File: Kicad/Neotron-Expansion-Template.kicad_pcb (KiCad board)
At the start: 2 copper layers, 100 x 50 mm, 26 parts, among them J1 Neotron-Expansion-Edge, SW1 SW_DIP_x08, U1 MCP23S17, U2 34LC02

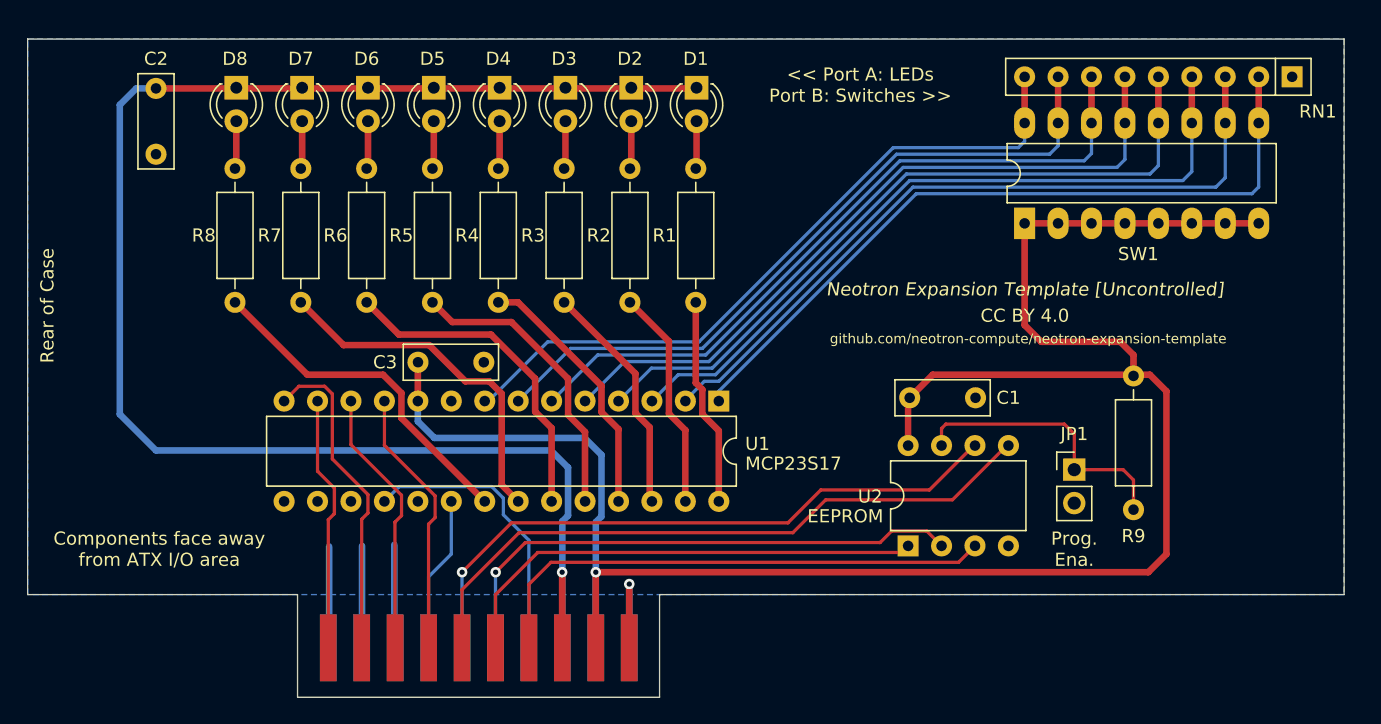
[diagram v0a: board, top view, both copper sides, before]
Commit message: Updated to KiCAD 6 and re-worked.
Power is the right way around now....
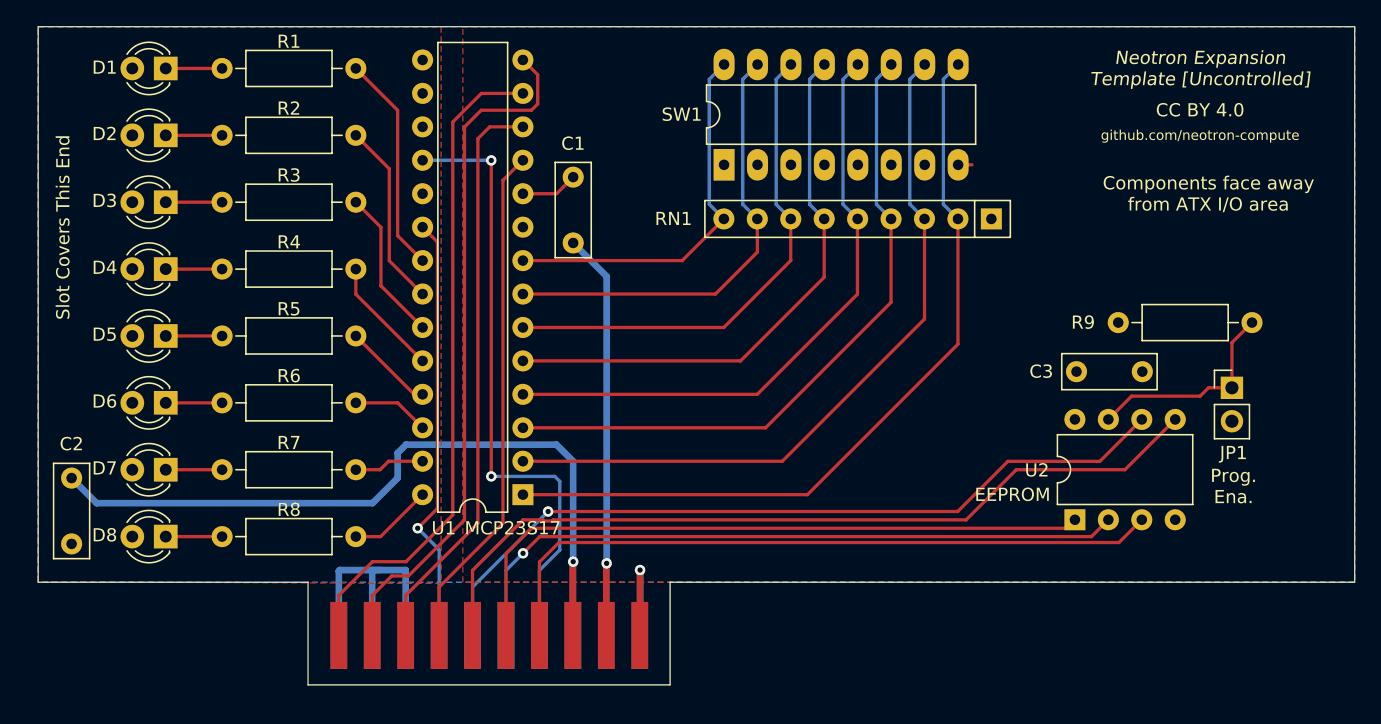
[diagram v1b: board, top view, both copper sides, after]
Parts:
- RN1: value 10k x 8 -> 10k
- moved D1 40.3 mm to (60.5, 102.2), turned to 180 degrees
- moved D2 35.5 mm to (60.5, 107.3), turned to 180 degrees
- moved D8 34.5 mm to (60.5, 137.8), turned to 180 degrees
- moved D3 31.6 mm to (60.5, 112.4), turned to 180 degrees
- moved R1 31.3 mm to (74.9, 102.2), turned to 180 degrees
- moved D7 30.8 mm to (60.5, 132.7), turned to 180 degrees
- moved C2 30.3 mm to (53.3, 133.3)
- moved D4 28.9 mm to (60.5, 117.5), turned to 180 degrees
- moved D6 28.4 mm to (60.5, 127.6), turned to 180 degrees
- moved D5 27.7 mm to (60.5, 122.6), turned to 180 degrees
- moved RN1 25.3 mm to (123.2, 113.7)
- moved R2 24.4 mm to (74.9, 107.3), turned to 180 degrees
- moved SW1 23.3 mm to (102.9, 109.6)
- moved R8 20.0 mm to (74.9, 137.8), turned to 180 degrees
- moved R3 17.6 mm to (74.9, 112.4), turned to 180 degrees
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- renumbered C3 to C1, C1 to C3
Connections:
- net /I2C_SCL renamed /SCL
- net /I2C_SDA renamed /SDA
- net Net-(J1-Pad1) renamed /COPI
- net Net-(J1-Pad14) renamed /~{RESET}
- net Net-(J1-Pad3) renamed /CIPO
- net Net-(J1-Pad5) renamed /CLK
- net Net-(J1-Pad7) renamed /~{CS}
- net Net-(J1-Pad8) renamed /~{IRQ}
- net Net-(JP1-Pad1) renamed /WP
- net Net-(RN1-Pad2) renamed /B0
- net Net-(RN1-Pad3) renamed /B1
- net Net-(RN1-Pad4) renamed /B2
- net Net-(RN1-Pad5) renamed /B3
- net Net-(RN1-Pad6) renamed /B4
- net Net-(RN1-Pad7) renamed /B5
- net Net-(RN1-Pad8) renamed /B6
- net Net-(RN1-Pad9) renamed /B7
- D1 pad 1: +5V -> Net-(R1-Pad2)
- D1 pad 2: Net-(D1-Pad2) -> +5V
- D2 pad 1: +5V -> Net-(D2-Pad1)
- D2 pad 2: Net-(D2-Pad2) -> +5V
- D3 pad 1: +5V -> Net-(D3-Pad1)
- D3 pad 2: Net-(D3-Pad2) -> +5V
- D4 pad 1: +5V -> Net-(D4-Pad1)
- D4 pad 2: Net-(D4-Pad2) -> +5V
- D5 pad 1: +5V -> Net-(D5-Pad1)
- D5 pad 2: Net-(D5-Pad2) -> +5V
- D6 pad 1: +5V -> Net-(D6-Pad1)
- D6 pad 2: Net-(D6-Pad2) -> +5V
- D7 pad 1: +5V -> Net-(D7-Pad1)
- D7 pad 2: Net-(D7-Pad2) -> +5V
- D8 pad 1: +5V -> Net-(D8-Pad1)
- D8 pad 2: Net-(D8-Pad2) -> +5V
- R1 pad 1: Net-(R1-Pad1) -> /A0
- R1 pad 2: Net-(D1-Pad2) -> Net-(R1-Pad2)
- R2 pad 1: Net-(R2-Pad1) -> /A1
- R2 pad 2: Net-(D2-Pad2) -> Net-(D2-Pad1)
- R3 pad 1: Net-(R3-Pad1) -> /A2
- R3 pad 2: Net-(D3-Pad2) -> Net-(D3-Pad1)
- R4 pad 1: Net-(R4-Pad1) -> /A3
- R4 pad 2: Net-(D4-Pad2) -> Net-(D4-Pad1)
- R5 pad 1: Net-(R5-Pad1) -> /A4
- R5 pad 2: Net-(D5-Pad2) -> Net-(D5-Pad1)
- R6 pad 1: Net-(R6-Pad1) -> /A5
- R6 pad 2: Net-(D6-Pad2) -> Net-(D6-Pad1)
- R7 pad 1: Net-(R7-Pad1) -> /A6
- R7 pad 2: Net-(D7-Pad2) -> Net-(D7-Pad1)
- R8 pad 1: Net-(R8-Pad1) -> /A7
- R8 pad 2: Net-(D8-Pad2) -> Net-(D8-Pad1)
- U1 pad 10: +3V3 -> GND
- U1 pad 19: (no net) -> unconnected-(U1-Pad19)
- U1 pad 21: Net-(R8-Pad1) -> /A0
- U1 pad 22: Net-(R7-Pad1) -> /A1
- U1 pad 23: Net-(R6-Pad1) -> /A2
- U1 pad 24: Net-(R5-Pad1) -> /A3
- U1 pad 25: Net-(R4-Pad1) -> /A4
- U1 pad 26: Net-(R3-Pad1) -> /A5
- U1 pad 27: Net-(R2-Pad1) -> /A6
- U1 pad 28: Net-(R1-Pad1) -> /A7
- U1 pad 9: GND -> +3V3
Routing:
- net +3V3: track 157.9 -> 37.4 mm
- net +5V: track 123.2 -> 61.2 mm
- net /COPI: track 19.5 -> 50.3 mm
- net /CIPO: track 25.0 -> 52.4 mm
- net Net-(R7-Pad1): track 26.9 -> 0.00 mm
- net Net-(R8-Pad1): track 26.3 -> 0.00 mm
- net Net-(R6-Pad1): track 25.0 -> 0.00 mm
- net /~{RESET}: track 22.0 -> 46.9 mm, vias 0 -> 2
- net /B7: track 54.1 -> 29.2 mm
- net /CLK: track 20.5 -> 43.8 mm
- net Net-(R5-Pad1): track 22.6 -> 0.00 mm
- net /~{IRQ}: track 11.8 -> 32.8 mm, vias 0 -> 1
- net /B6: track 54.3 -> 34.3 mm
- net Net-(R4-Pad1): track 19.8 -> 0.00 mm
- net /~{CS}: track 20.5 -> 38.7 mm
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- added copper zone on F.Cu, net +3V3
- added copper zone on F.Cu, net +5V
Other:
- net class Default removed
- board text added: "Slot Covers This End"
- board text added: "github.com/neotron-compute"
- board text removed: "<< Port A: LEDs Port B: Switches >>"
- board text removed: "Rear of Case"
- board text removed: "github.com/neotron-compute/neotron-expansion-template"

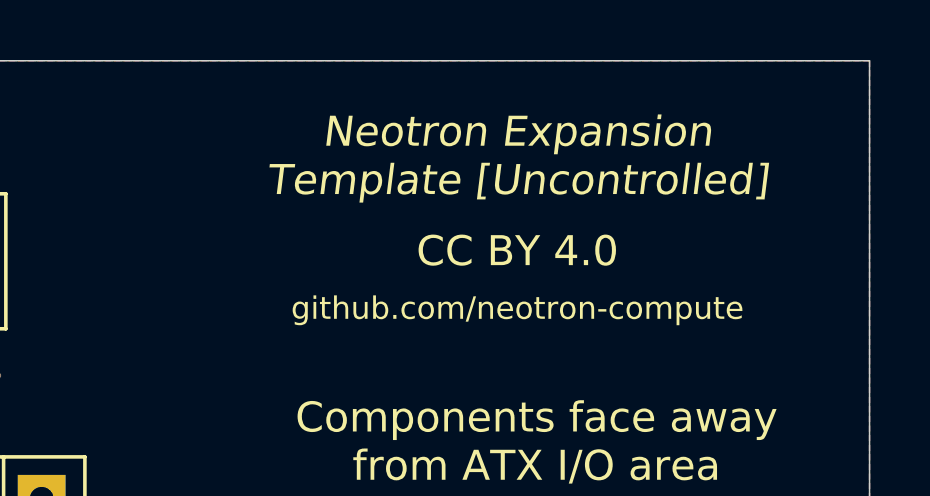
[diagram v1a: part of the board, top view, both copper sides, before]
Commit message: Fix date/version fields.
They must be set as ${field}, so Kibot can replace them.
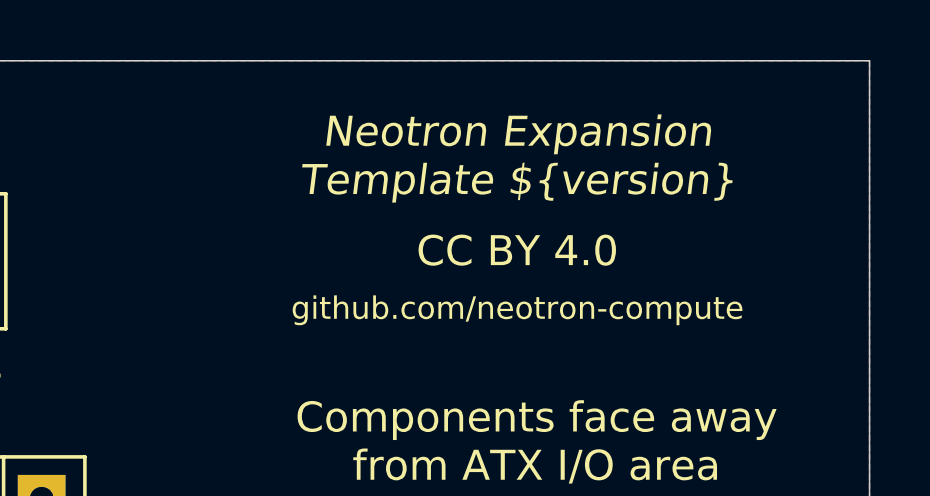
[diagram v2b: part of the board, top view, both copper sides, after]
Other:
- board text added: "Neotron Expansion Template ${version}"
- board text removed: "Neotron Expansion Template [Uncontrolled]"
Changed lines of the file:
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@@
   (title_block
     (title "Neotron Expansion Template")
-    (date "2021-08-18")
-    (rev "[Uncontrolled]")
+    (date "${date}")
+    (rev "${version}")
     (company "https://neotron-compute.github.io/")
     (comment 1 "Licenced as CC BY 4.0")
-    (comment 2 "Copyright (c) 2021 The Neotron Developers, et al")
+    (comment 2 "Copyright (c) 2022 The Neotron Developers")
   )
   (layers
@@
     (effects (font (size 1 1) (thickness 0.15)))
   )
-  (gr_text "Neotron Expansion\nTemplate [Uncontrolled]" (at 139.065 102.235) (layer "F.SilkS")
+  (gr_text "Neotron Expansion\nTemplate ${version}" (at 139.065 102.235) (layer "F.SilkS")
     (effects (font (size 1 1) (thickness 0.15) italic))
   )

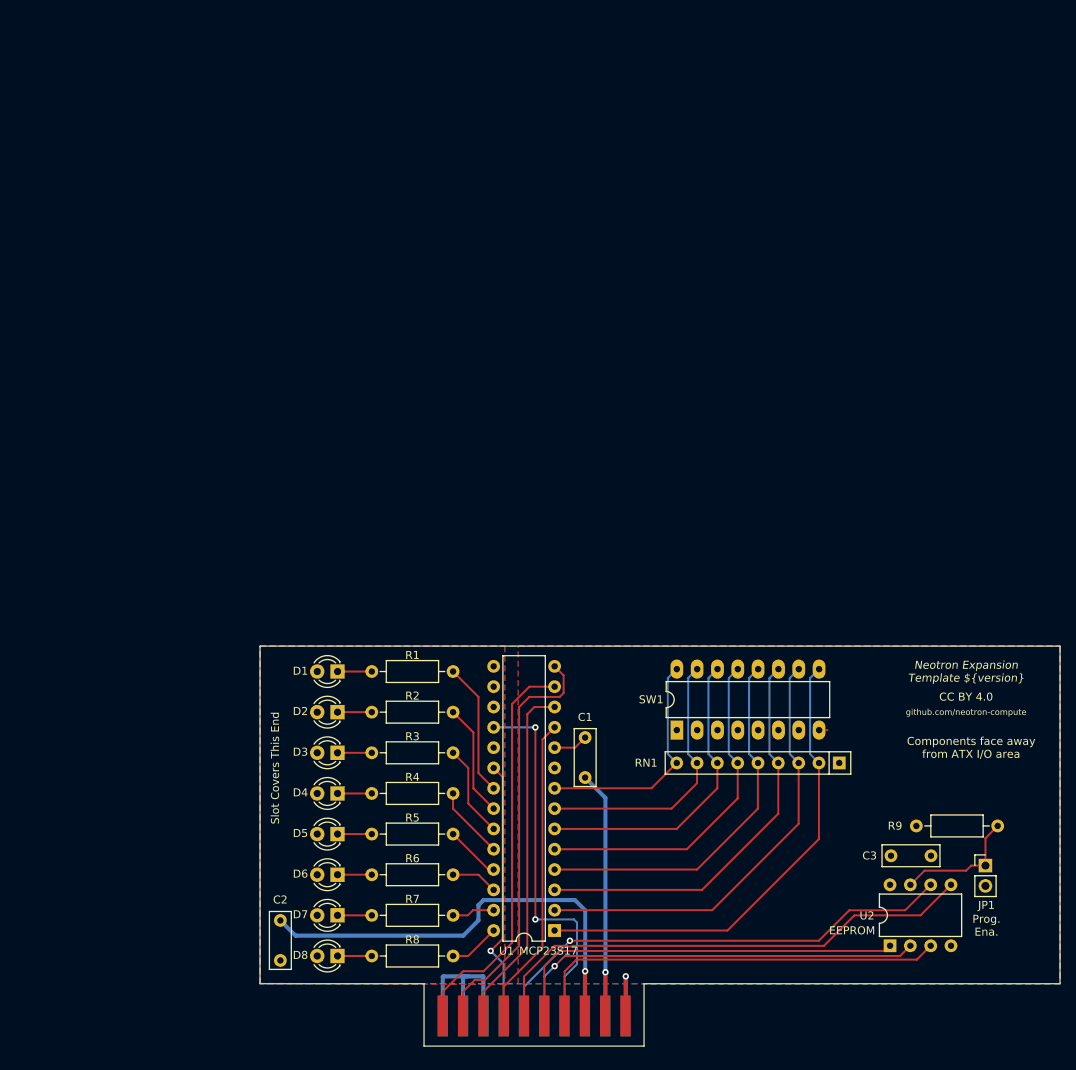
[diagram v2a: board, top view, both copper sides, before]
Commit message: Adjusted board size to suit Neotron Pico 1.0.0.
Has holes for a random backplate I found.
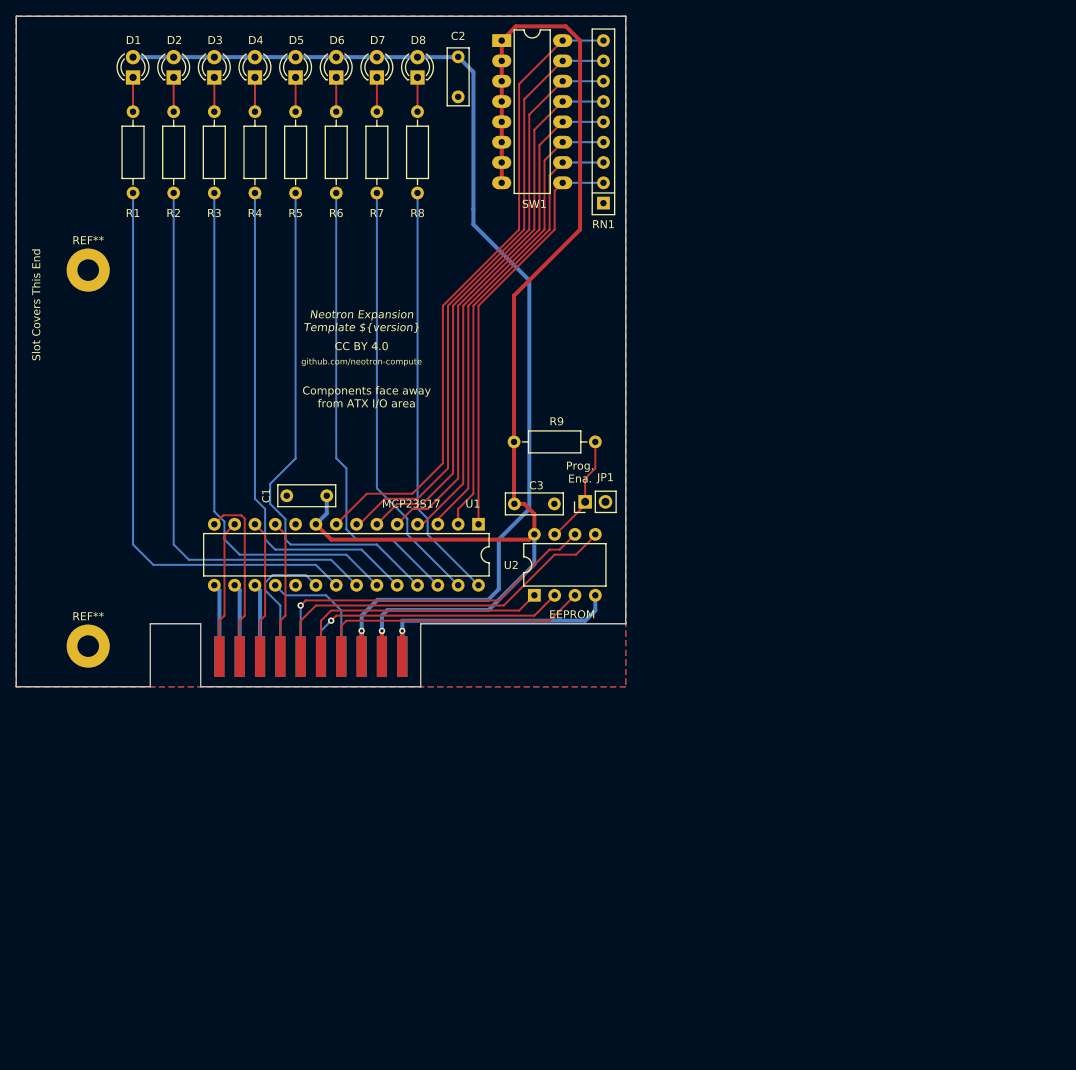
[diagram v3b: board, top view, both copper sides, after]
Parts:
- added REF**: MountingHole_2.7mm_M2.5_Pad, MountingHole:MountingHole_2.7mm_M2.5_Pad, F.Cu at (29.3, 99.1)
- added REF**: MountingHole_2.7mm_M2.5_Pad, MountingHole:MountingHole_2.7mm_M2.5_Pad, F.Cu at (29.3, 52.1)
- moved D8 110.3 mm to (70.5, 28.0), turned to 90 degrees
- moved C2 110.2 mm to (75.6, 25.4)
- moved D7 104.9 mm to (65.4, 28.0), turned to 90 degrees
- moved D6 99.7 mm to (60.3, 28.0), turned to 90 degrees
- moved R8 95.5 mm to (70.5, 42.4), turned to 90 degrees
- moved D5 94.7 mm to (55.2, 28.0), turned to 90 degrees
- moved R7 90.8 mm to (65.4, 42.4), turned to 90 degrees
- moved D4 90.1 mm to (50.2, 28.0), turned to 90 degrees
- moved SW1 88.9 mm to (81.0, 23.4), turned to 0 degrees
- moved R6 86.5 mm to (60.3, 42.4), turned to 90 degrees
- moved D3 85.8 mm to (45.1, 28.0), turned to 90 degrees
- moved R5 82.5 mm to (55.2, 42.4), turned to 90 degrees
- moved D2 81.9 mm to (40.0, 28.0), turned to 90 degrees
- moved R4 79.0 mm to (50.2, 42.4), turned to 90 degrees
- moved D1 78.5 mm to (34.9, 28.0), turned to 90 degrees
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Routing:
- net +3V3: track 37.4 -> 161.6 mm
- net +5V: track 61.2 -> 139.3 mm
- net /A4: track 6.27 -> 64.3 mm
- net /A1: track 14.2 -> 68.9 mm
- net /A0: track 16.7 -> 71.5 mm
- net /A3: track 9.08 -> 63.6 mm
- net /A2: track 11.6 -> 65.3 mm
- net /A5: track 5.85 -> 56.9 mm
- net /B7: track 29.2 -> 80.1 mm
- net /A6: track 5.34 -> 53.2 mm
- net /A7: track 6.39 -> 52.2 mm
- net /B6: track 34.3 -> 75.9 mm
- net /B5: track 38.3 -> 71.4 mm
- net /COPI: track 50.3 -> 17.3 mm
- net /~{RESET}: track 46.9 -> 15.3 mm, vias 2 -> 0
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- added copper zone on F.Cu, net GND
- removed copper zone on F.Cu, net +3V3
- removed copper zone on F.Cu, net +5V
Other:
- board size 100 x 50 mm -> 76.2 x 83.8 mm

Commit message: Fix DRC issues.
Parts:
- H1, H2: renamed from REF**; value MountingHole_2.7mm_M2.5_Pad -> MountingHole_Pad
- R1: value 330 -> 10k
- R9: value 10k -> 330
- moved R1 65.7 mm to (92.7, 73.7), turned to 180 degrees
- moved C2 56.3 mm to (82.6, 81.3), turned to 0 degrees
- moved C3 56.3 mm to (75.6, 25.4), turned to -90 degrees
- moved R9 38.2 mm to (70.5, 42.4), turned to 90 degrees
- moved R2 5.08 mm to (34.9, 42.4)
- moved R6 5.08 mm to (55.2, 42.4)
- moved R3 5.08 mm to (40.0, 42.4)
- moved R4 5.08 mm to (45.1, 42.4)
- moved R5 5.08 mm to (50.2, 42.4)
- moved R7 5.08 mm to (60.3, 42.4)
- moved R8 5.08 mm to (65.4, 42.4)
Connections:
- C2 pad 1: +5V -> +3V3
- C3 pad 1: +3V3 -> +5V
- H1 pad 1: (no net) -> GND
- H2 pad 1: (no net) -> GND
- R1 pad 1: /A0 -> /WP
- R1 pad 2: Net-(D1-Pad1) -> +3V3
- R2 pad 1: /A1 -> /A0
- R2 pad 2: Net-(D2-Pad1) -> Net-(D1-Pad1)
- R3 pad 1: /A2 -> /A1
- R3 pad 2: Net-(D3-Pad1) -> Net-(D2-Pad1)
- R4 pad 1: /A3 -> /A2
- R4 pad 2: Net-(D4-Pad1) -> Net-(D3-Pad1)
- R5 pad 1: /A4 -> /A3
- R5 pad 2: Net-(D5-Pad1) -> Net-(D4-Pad1)
- R6 pad 1: /A5 -> /A4
- R6 pad 2: Net-(D6-Pad1) -> Net-(D5-Pad1)
- R7 pad 1: /A6 -> /A5
- R7 pad 2: Net-(D7-Pad1) -> Net-(D6-Pad1)
- R8 pad 1: /A7 -> /A6
- R8 pad 2: Net-(D8-Pad1) -> Net-(D7-Pad1)
- R9 pad 1: /WP -> /A7
- R9 pad 2: +3V3 -> Net-(D8-Pad1)
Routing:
- net /A2: track 65.3 -> 67.8 mm
- net /A3: track 63.6 -> 64.3 mm
